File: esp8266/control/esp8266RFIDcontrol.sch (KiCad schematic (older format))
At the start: 20 parts, among them J1 C_DOOR, J2 C_STRIKE, J3 Conn_01x05, J4 C_PWR, K1 RTE24005F, Q1 Q_PNP_CBE, SW1 SW_RESET, U1 TPS561208, U2 LoLinESP8266

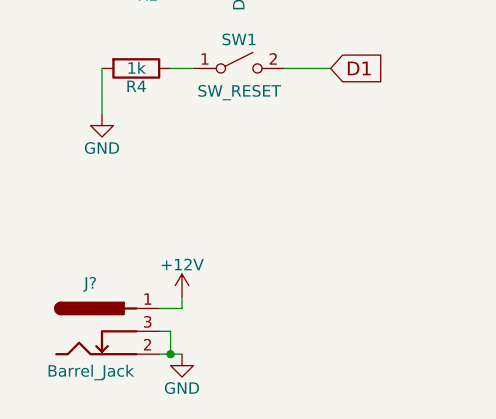
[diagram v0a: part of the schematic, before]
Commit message: ESP8266 RFID reader board
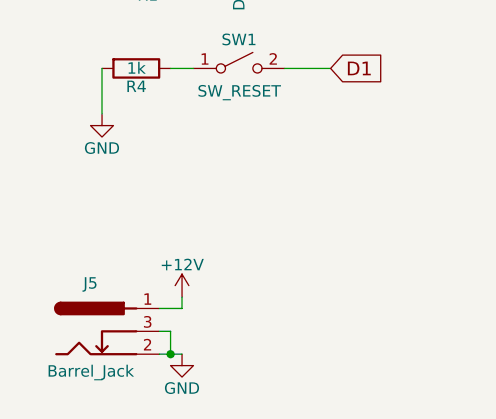
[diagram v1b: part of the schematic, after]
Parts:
- J5: renamed from J?; footprint (none) -> Connectors:BARREL_JACK
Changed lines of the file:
@@
 	8600 1950 7800 1950
 $Comp
-L Barrel_Jack J?
+L Barrel_Jack J5
 U 1 1 5B26EC40
 P 1400 5300
-F 0 "J?" H 1400 5510 50  0000 C CNN
+F 0 "J5" H 1400 5510 50  0000 C CNN
 F 1 "Barrel_Jack" H 1400 5125 50  0000 C CNN
-F 2 "" H 1450 5260 50  0001 C CNN
+F 2 "Connectors:BARREL_JACK" H 1450 5260 50  0001 C CNN
 F 3 "" H 1450 5260 50  0001 C CNN
 	1    1400 5300
@@
 $EndComp
 $Comp
-L GND #PWR?
+L GND #PWR020
 U 1 1 5B26F00B
 P 1800 5400
-F 0 "#PWR?" H 1800 5150 50  0001 C CNN
+F 0 "#PWR020" H 1800 5150 50  0001 C CNN
 F 1 "GND" H 1800 5250 50  0000 C CNN
 F 2 "" H 1800 5400 50  0001 C CNN
@@
 Connection ~ 1750 5400
 $Comp
-L +12V #PWR?
+L +12V #PWR021
 U 1 1 5B26F5F6
 P 1800 5150
-F 0 "#PWR?" H 1800 5000 50  0001 C CNN
+F 0 "#PWR021" H 1800 5000 50  0001 C CNN
 F 1 "+12V" H 1800 5290 50  0000 C CNN
 F 2 "" H 1800 5150 50  0001 C CNN
